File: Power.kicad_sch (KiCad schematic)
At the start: 25 parts, among them J2 USB_C_Receptacle_USB2.0_16P, J3 Conn_01x02, Q1 AO3401A, Q3 AO3401A, U3 CN3063, U4 TLV74033PDBVR, U5 CH340N, U6 TPS7A0533PDBV, U8 TPS3839K33DBZ

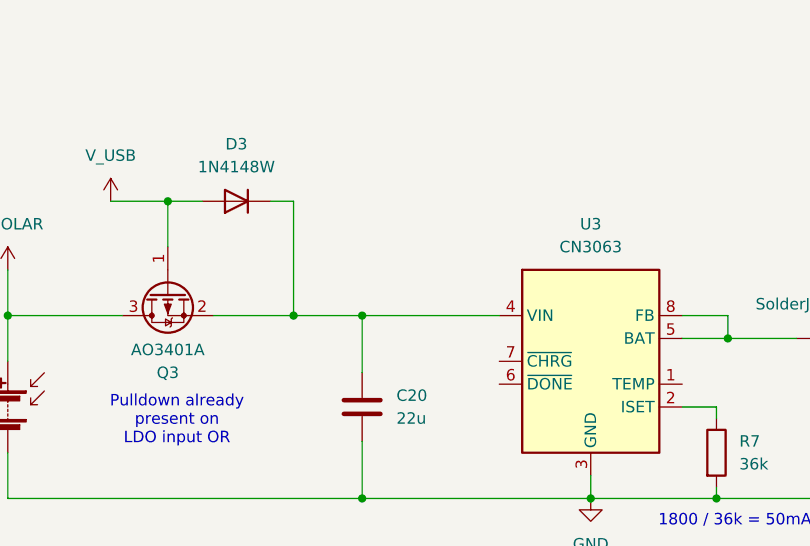
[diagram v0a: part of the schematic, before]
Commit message: add CHG and DONE LEDs for CN3063
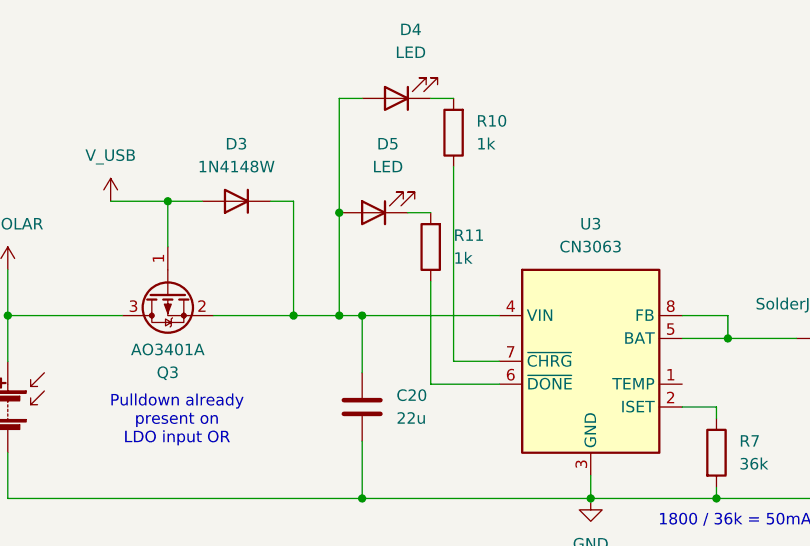
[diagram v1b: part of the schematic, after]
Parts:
- added D4, D5: LED, LED_SMD:LED_0603_1608Metric_Pad1.05x0.95mm_HandSolder, symbol Device:LED
- added R10, R11: 1k, Resistor_SMD:R_0603_1608Metric_Pad0.98x0.95mm_HandSolder, symbol Device:R
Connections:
- net at C20.1, D3.1 (K), Q3.2 (S)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: now also D4.2 (A), D5.2 (A)
- net at U3.6 (~{DONE}): now also R11.1
- net at U3.7 (~{CHRG}): now also R10.1
- new net: D5.1 (K), R11.2
- new net: D4.1 (K), R10.2

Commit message: change CN3063 input diode and tie temp to ground, HW UVP LPF, change DCDC input capacitance setup, remove crystal loading caps, add series resistors on CH340 serial lines, add via fence on CPWGs
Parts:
- added C31: 1u, Capacitor_SMD:C_0603_1608Metric_Pad1.08x0.95mm_HandSolder, symbol Device:C
- added R12, R13: 330, Resistor_SMD:R_0603_1608Metric_Pad0.98x0.95mm_HandSolder, symbol Device:R
- added R14: 10k, Resistor_SMD:R_0603_1608Metric_Pad0.98x0.95mm_HandSolder, symbol Device:R
- C25: value 22u -> 4.7u
- D3: value 1N4148W -> B5819W
- R8: value 36k -> 5.1k
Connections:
- net GND: now also U3.1 (TEMP), C31.2
- net VCOM_RX: now also R13.2; no longer U5.7 (RXD)
- net VCOM_TX: now also R12.2; no longer U5.6 (TXD)
- net V_BAT: now also R14.1; no longer U8.3 (VDD)
- new net: R13.1, U5.7 (RXD)
- new net: R12.1, U5.6 (TXD)
- new net: C31.1, R14.2, U8.3 (VDD)
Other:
- note added: "10ms time constant"
- note added: "TEMP groudned to disable"

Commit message: add LCSC part number properties in preparation for JLCPCB assembly order
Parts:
- C20, C22, C25: LCSC Part Number (none) -> C1779
- C21, C23, C24, C31: LCSC Part Number (none) -> C15849
- D2: LCSC Part Number (none) -> C81598
- D3: LCSC Part Number (none) -> C8598
- J2: LCSC Part Number (none) -> C165948
- Q1, Q3: LCSC Part Number (none) -> C15127
- R10, R11: LCSC Part Number (none) -> C21190
- R12, R13: LCSC Part Number (none) -> C23138
- R14: LCSC Part Number (none) -> C25804
- R5, R6, R8: LCSC Part Number (none) -> C23186
- R7: LCSC Part Number (none) -> C23153
- U3: LCSC Part Number (none) -> C28078
- U4: LCSC Part Number (none) -> C3743587
- U5: LCSC Part Number (none) -> C2977777
- U6: LCSC Part Number (none) -> C493453
- U8: LCSC Part Number (none) -> C96333
